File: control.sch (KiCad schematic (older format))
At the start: 1 part

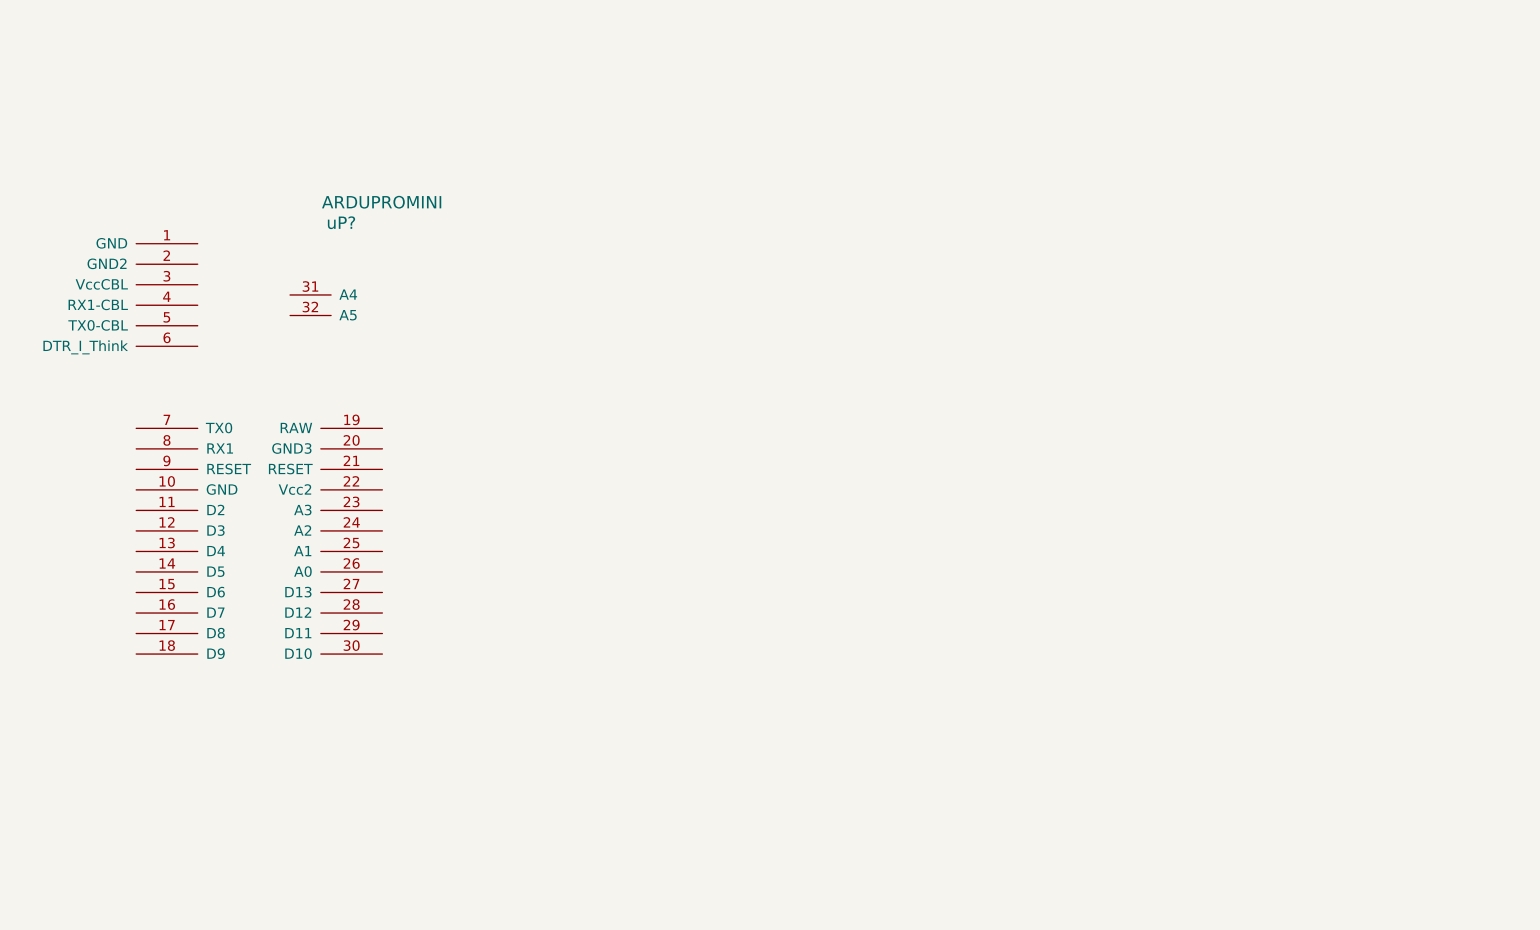
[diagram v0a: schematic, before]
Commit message: Schematic v0.2
Added IC and wiring
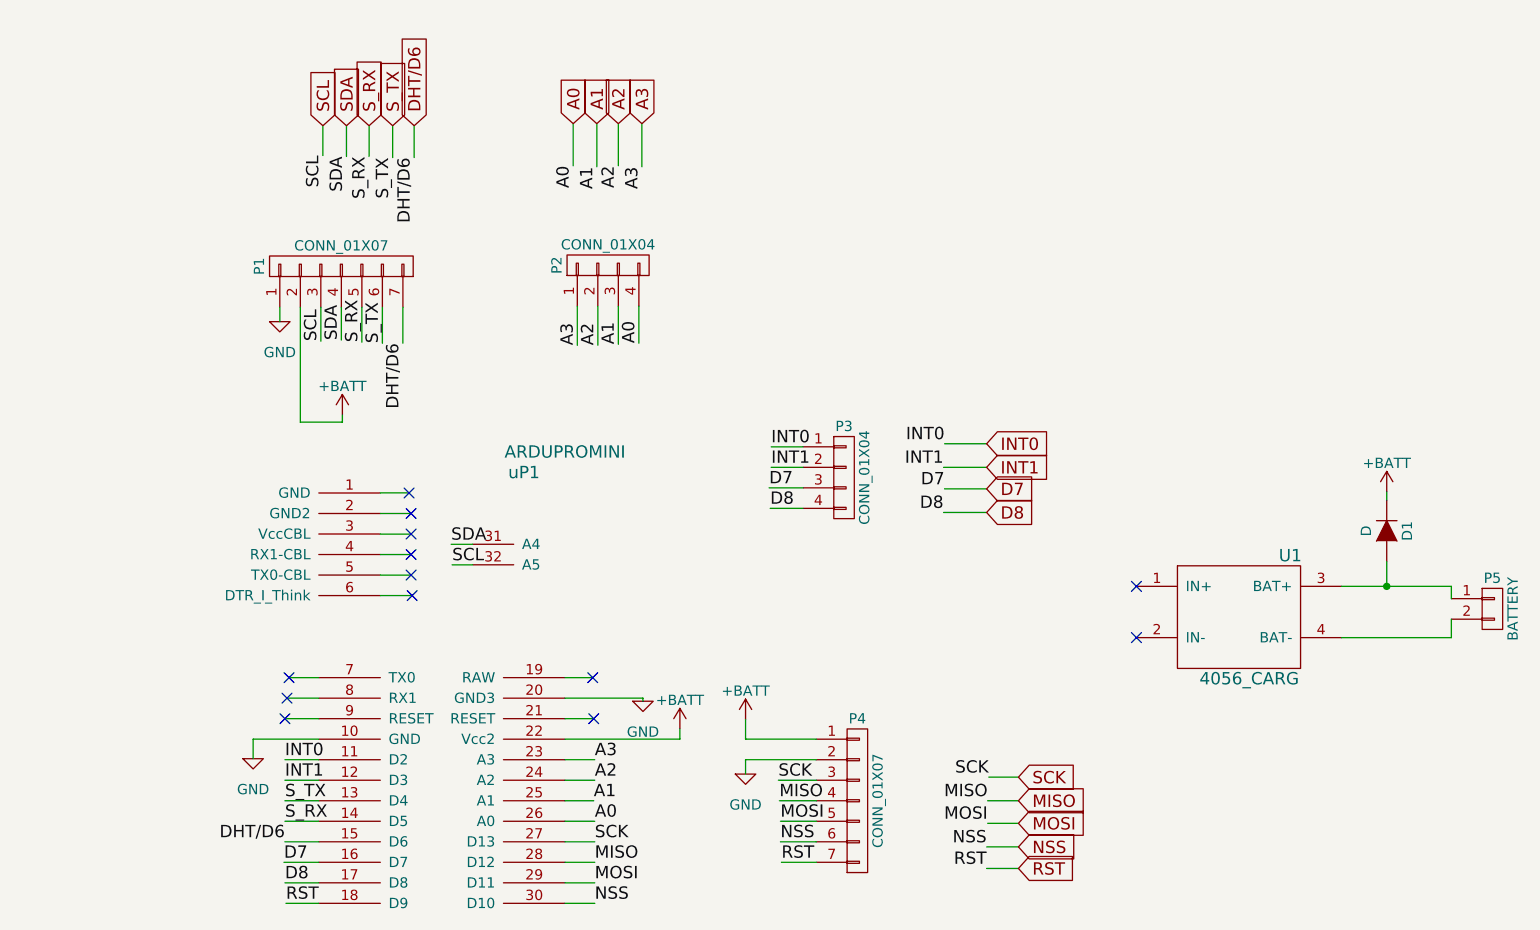
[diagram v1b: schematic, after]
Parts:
- added D1: D, symbol D
- added P1, P4: CONN_01X07, symbol CONN_01X07
- added P2, P3: CONN_01X04, symbol CONN_01X04
- added P5: BATTERY, symbol CONN_01X02
- added U1: 4056_CARG, symbol 4056_CARG
- gave numbers to parts that had none: 1
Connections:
- net GND: now reaches uP1.10 (GND)
- net GND: now also uP1.20 (GND3), P1.1 (P1), P4.2 (P2)
- net INT0: now reaches uP1.11 (D2)
- net INT0: now also P3.1 (P1)
- net INT1: now reaches uP1.12 (D3)
- net INT1: now also P3.2 (P2)
- net S_TX: now reaches uP1.13 (D4)
- net S_TX: now also P1.6 (P6)
- net S_RX: now reaches uP1.14 (D5)
- net S_RX: now also P1.5 (P5)
- net DHT/D6: now reaches uP1.15 (D6)
- net DHT/D6: now also P1.7 (P7)
- net D7: now reaches uP1.16 (D7)
- net D7: now also P3.3 (P3)
- net D8: now reaches uP1.17 (D8)
- net D8: now also P3.4 (P4)
- net RST: now reaches uP1.18 (D9)
- net RST: now also P4.7 (P7)
- net +BATT: now reaches uP1.22 (Vcc2)
- net +BATT: now also D1.1 (K), P1.2 (P2), P4.1 (P1)
- net A3: now reaches uP1.23 (A3)
- net A3: now also P2.1 (P1)
- net A2: now reaches uP1.24 (A2)
- net A2: now also P2.2 (P2)
- net A1: now reaches uP1.25 (A1)
- net A1: now also P2.3 (P3)
- net A0: now reaches uP1.26 (A0)
- net A0: now also P2.4 (P4)
- net SCK: now reaches uP1.27 (D13)
- net SCK: now also P4.3 (P3)
- net MISO: now reaches uP1.28 (D12)
- net MISO: now also P4.4 (P4)
- net MOSI: now reaches uP1.29 (D11)
- net MOSI: now also P4.5 (P5)
- net NSS: now reaches uP1.30 (D10)
- net NSS: now also P4.6 (P6)
- net SDA: now reaches uP1.31 (A4)
- net SDA: now also P1.4 (P4)
- net SCL: now reaches uP1.32 (A5)
- net SCL: now also P1.3 (P3)
- new net: D1.2 (A), P5.1 (P1), U1.3 (BAT+)
- new net: P5.2 (P2), U1.4 (BAT-)
- no-connect marks 0 -> 13
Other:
- moved on the sheet: uP1

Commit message: Fix arduino mini pro pin 6 bug, added capacitors
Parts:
- added C1: C, symbol C
- D1: footprint (none) -> Diodes_ThroughHole:Diode_DO-41_SOD81_Horizontal_RM10
- P1, P4: footprint (none) -> Pin_Headers:Pin_Header_Straight_1x07
- P2, P3: footprint (none) -> Pin_Headers:Pin_Header_Straight_1x04
- P5: footprint (none) -> Pin_Headers:Pin_Header_Straight_1x02
- RAW1: renamed from uP1; footprint (none) -> CatSat:arduinoMiniPro
- U1: footprint (none) -> CatSat:4056_lipoCharg
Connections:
- net +BATT: now also C1.1
- net GND: now also C1.2
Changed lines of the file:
@@
 EESchema Schematic File Version 2
+LIBS:CatSat-rescue
 LIBS:power
 LIBS:device
@@
 LIBS:contrib
 LIBS:valves
-LIBS:ArduProMiniTKB
-LIBS:L80-M39
-LIBS:RFM95W-868S2
-LIBS:theinventorhouse
 LIBS:CatSat-cache
+LIBS:rfm95
 EELAYER 25 0
 EELAYER END
@@
 F 0 "P2" H 4435 2285 50  0000 C CNN
 F 1 "CONN_01X04" V 4535 2035 50  0000 C CNN
-F 2 "" H 4435 2035 50  0000 C CNN
+F 2 "Pin_Headers:Pin_Header_Straight_1x04" H 4435 2035 50  0001 C CNN
 F 3 "" H 4435 2035 50  0000 C CNN
 	1    4435 2035
@@
 F 0 "P1" H 3135 2440 50  0000 C CNN
 F 1 "CONN_01X07" V 3235 2040 50  0000 C CNN
-F 2 "" H 3135 2040 50  0000 C CNN
+F 2 "Pin_Headers:Pin_Header_Straight_1x07" H 3135 2040 50  0001 C CNN
 F 3 "" H 3135 2040 50  0000 C CNN
 	1    3135 2040
@@
 F 0 "P4" H 5650 5045 50  0000 C CNN
 F 1 "CONN_01X07" V 5750 4645 50  0000 C CNN
-F 2 "" H 5650 4645 50  0000 C CNN
+F 2 "Pin_Headers:Pin_Header_Straight_1x07" H 5650 4645 50  0001 C CNN
 F 3 "" H 5650 4645 50  0000 C CNN
 	1    5650 4645
@@
 F 0 "P3" H 5585 3320 50  0000 C CNN
 F 1 "CONN_01X04" V 5685 3070 50  0000 C CNN
-F 2 "" H 5585 3070 50  0000 C CNN
+F 2 "Pin_Headers:Pin_Header_Straight_1x04" H 5585 3070 50  0001 C CNN
 F 3 "" H 5585 3070 50  0000 C CNN
 	1    5585 3070
@@
 NoConn ~ 3480 3645
 $Comp
-L ARDUPROMINI uP1
+L ARDUPROMINI RAW1
 U 1 1 579665C1
 P 4225 2945
-F 0 "uP1" H 4025 2845 60  0000 C CNN
+F 0 "RAW1" H 4025 2845 60  0000 C CNN
 F 1 "ARDUPROMINI" H 4225 2945 60  0000 C CNN
-F 2 "" H 4225 2945 60  0000 C CNN
+F 2 "CatSat:arduinoMiniPro" H 4225 2945 60  0001 C CNN
 F 3 "" H 4225 2945 60  0000 C CNN
 	1    4225 2945
@@
 U 1 1 579865C8
 P 4605 4160
+AR Path="/579865C8" Ref="#PWR03"  Part="1"
+AR Path="/57965E31/579865C8" Ref="#PWR03"  Part="1"
 F 0 "#PWR03" H 4605 3910 50  0001 C CNN
 F 1 "GND" H 4605 4010 50  0000 C CNN
@@
 U 1 1 579869BC
 P 2705 4440
+AR Path="/579869BC" Ref="#PWR04"  Part="1"
+AR Path="/57965E31/579869BC" Ref="#PWR04"  Part="1"
 F 0 "#PWR04" H 2705 4190 50  0001 C CNN
 F 1 "GND" H 2705 4290 50  0000 C CNN
@@
 F 0 "U1" H 7760 4050 60  0000 C CNN
 F 1 "4056_CARG" H 7560 3450 60  0000 C CNN
-F 2 "" H 7510 3750 60  0000 C CNN
+F 2 "CatSat:4056_lipoCharg" H 7510 3750 60  0001 C CNN
 F 3 "" H 7510 3750 60  0000 C CNN
 	1    7510 3750
@@
 F 0 "P5" H 8745 3860 50  0000 C CNN
 F 1 "BATTERY" V 8845 3710 50  0000 C CNN
-F 2 "" H 8745 3710 50  0000 C CNN
+F 2 "Pin_Headers:Pin_Header_Straight_1x02" H 8745 3710 50  0001 C CNN
 F 3 "" H 8745 3710 50  0000 C CNN
 	1    8745 3710
@@
 F 0 "D1" H 8230 3430 50  0000 C CNN
 F 1 "D" H 8230 3230 50  0000 C CNN
-F 2 "" H 8230 3330 50  0000 C CNN
+F 2 "Diodes_ThroughHole:Diode_DO-41_SOD81_Horizontal_RM10" H 8230 3330 50  0001 C CNN
 F 3 "" H 8230 3330 50  0000 C CNN
 	1    8230 3330
@@
 U 1 1 5798B584
 P 2835 2310
+AR Path="/5798B584" Ref="#PWR06"  Part="1"
+AR Path="/57965E31/5798B584" Ref="#PWR06"  Part="1"
 F 0 "#PWR06" H 2835 2060 50  0001 C CNN
 F 1 "GND" H 2835 2160 50  0000 C CNN
@@
 U 1 1 579A7004
 P 5105 4515
+AR Path="/579A7004" Ref="#PWR07"  Part="1"
+AR Path="/57965E31/579A7004" Ref="#PWR07"  Part="1"
 F 0 "#PWR07" H 5105 4265 50  0001 C CNN
 F 1 "GND" H 5105 4365 50  0000 C CNN
@@
 Wire Wire Line
 	5105 4345 5105 4250
+$Comp
+L C C1
+U 1 1 579BC305
+P 6955 2585
+F 0 "C1" H 6980 2685 50  0000 L CNN
+F 1 "C" H 6980 2485 50  0000 L CNN
+F 2 "" H 6993 2435 30  0000 C CNN
+F 3 "" H 6955 2585 60  0000 C CNN
+	1    6955 2585
+	1    0    0    -1
+$EndComp
+$Comp
+L +BATT #PWR?
+U 1 1 579BC449
+P 6955 2385
+F 0 "#PWR?" H 6955 2235 50  0001 C CNN
+F 1 "+BATT" H 6955 2525 50  0000 C CNN
+F 2 "" H 6955 2385 50  0000 C CNN
+F 3 "" H 6955 2385 50  0000 C CNN
+	1    6955 2385
+	1    0    0    -1
+$EndComp
+$Comp
+L GND #PWR?
+U 1 1 579BC6D3
+P 6955 2785
+AR Path="/579BC6D3" Ref="#PWR?"  Part="1"
+AR Path="/57965E31/579BC6D3" Ref="#PWR?"  Part="1"
+F 0 "#PWR?" H 6955 2535 50  0001 C CNN
+F 1 "GND" H 6955 2635 50  0000 C CNN
+F 2 "" H 6955 2785 50  0000 C CNN
+F 3 "" H 6955 2785 50  0000 C CNN
+	1    6955 2785
+	1    0    0    -1
+$EndComp
+Wire Wire Line
+	6955 2735 6955 2785
+Wire Wire Line
+	6955 2385 6955 2435
 $EndSCHEMATC

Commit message: Finished telemtry PCB
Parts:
- C1: footprint (none) -> Capacitors_ThroughHole:C_Disc_D6_P5
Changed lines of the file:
@@
 F 0 "C1" H 6980 2685 50  0000 L CNN
 F 1 "C" H 6980 2485 50  0000 L CNN
-F 2 "" H 6993 2435 30  0000 C CNN
+F 2 "Capacitors_ThroughHole:C_Disc_D6_P5" H 6993 2435 30  0001 C CNN
 F 3 "" H 6955 2585 60  0000 C CNN
 	1    6955 2585
@@
 $EndComp
 $Comp
-L +BATT #PWR?
+L +BATT #PWR09
 U 1 1 579BC449
 P 6955 2385
-F 0 "#PWR?" H 6955 2235 50  0001 C CNN
+F 0 "#PWR09" H 6955 2235 50  0001 C CNN
 F 1 "+BATT" H 6955 2525 50  0000 C CNN
 F 2 "" H 6955 2385 50  0000 C CNN
@@
 P 6955 2785
 AR Path="/579BC6D3" Ref="#PWR?"  Part="1"
-AR Path="/57965E31/579BC6D3" Ref="#PWR?"  Part="1"
-F 0 "#PWR?" H 6955 2535 50  0001 C CNN
+AR Path="/57965E31/579BC6D3" Ref="#PWR010"  Part="1"
+F 0 "#PWR010" H 6955 2535 50  0001 C CNN
 F 1 "GND" H 6955 2635 50  0000 C CNN
 F 2 "" H 6955 2785 50  0000 C CNN

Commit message: PCB final
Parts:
- added P0n1: ON, Pin_Headers:Pin_Header_Straight_1x02, symbol CONN_01X02
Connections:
- net +BATT: now also P0n1.1 (P1); no longer D1.1 (K)
- new net: D1.1 (K), P0n1.2 (P2)
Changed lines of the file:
@@
 L D D1
 U 1 1 579882B5
-P 8230 3330
-F 0 "D1" H 8230 3430 50  0000 C CNN
-F 1 "D" H 8230 3230 50  0000 C CNN
-F 2 "Diodes_ThroughHole:Diode_DO-41_SOD81_Horizontal_RM10" H 8230 3330 50  0001 C CNN
-F 3 "" H 8230 3330 50  0000 C CNN
-	1    8230 3330
+P 8225 3340
+F 0 "D1" H 8225 3440 50  0000 C CNN
+F 1 "D" H 8225 3240 50  0000 C CNN
+F 2 "Diodes_ThroughHole:Diode_DO-41_SOD81_Horizontal_RM10" H 8225 3340 50  0001 C CNN
+F 3 "" H 8225 3340 50  0000 C CNN
+	1    8225 3340
 	0    1    1    0
 $EndComp
@@
 L +BATT #PWR05
 U 1 1 5798845B
-P 8230 3140
-F 0 "#PWR05" H 8230 2990 50  0001 C CNN
-F 1 "+BATT" H 8230 3280 50  0000 C CNN
-F 2 "" H 8230 3140 50  0000 C CNN
-F 3 "" H 8230 3140 50  0000 C CNN
-	1    8230 3140
+P 8260 2875
+F 0 "#PWR05" H 8260 2725 50  0001 C CNN
+F 1 "+BATT" H 8260 3015 50  0000 C CNN
+F 2 "" H 8260 2875 50  0000 C CNN
+F 3 "" H 8260 2875 50  0000 C CNN
+	1    8260 2875
 	1    0    0    -1
 $EndComp
@@
 	4785 4345 4785 4295
 Wire Wire Line
-	8010 3600 8545 3600
-Wire Wire Line
 	8545 3600 8545 3660
 Wire Wire Line
@@
 Wire Wire Line
 	8545 3850 8010 3850
-Connection ~ 8230 3600
-Wire Wire Line
-	8230 3480 8230 3600
-Wire Wire Line
-	8230 3600 8235 3600
-Wire Wire Line
-	8230 3140 8230 3180
+Wire Wire Line
+	8235 3600 8230 3600
+Wire Wire Line
+	8260 2875 8260 2995
 Wire Wire Line
 	2935 2240 2935 2800
@@
 Wire Wire Line
 	6955 2385 6955 2435
+Wire Wire Line
+	8235 3490 8235 3600
+Connection ~ 8235 3600
+Wire Wire Line
+	8010 3600 8545 3600
+$Comp
+L CONN_01X02 P0n1
+U 1 1 57A00135
+P 8470 3045
+F 0 "P0n1" H 8470 3195 50  0000 C CNN
+F 1 "ON" V 8570 3045 50  0000 C CNN
+F 2 "Pin_Headers:Pin_Header_Straight_1x02" H 8470 3045 50  0001 C CNN
+F 3 "" H 8470 3045 50  0000 C CNN
+	1    8470 3045
+	1    0    0    -1
+$EndComp
+Wire Wire Line
+	8260 2995 8270 2995
+Wire Wire Line
+	8270 3095 8225 3095
+Wire Wire Line
+	8225 3095 8225 3190
+Wire Wire Line
+	8235 3490 8225 3490
 $EndSCHEMATC

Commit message: Fix Source Track
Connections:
- net GND: now also P5.2 (P2), U1.4 (BAT-)
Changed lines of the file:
@@
 LIBS:valves
 LIBS:CatSat-cache
-LIBS:rfm95
 EELAYER 25 0
 EELAYER END
@@
 encoding utf-8
 Sheet 2 4
-Title ""
-Date "2016-07-26"
+Title "CatSat v1.0"
+Date "2016-08-10"
 Rev "0.2"
 Comp "Electronic Cats"
@@
 Wire Wire Line
 	8235 3490 8225 3490
+$Comp
+L GND #PWR?
+U 1 1 57AC0CD8
+P 8180 4085
+F 0 "#PWR?" H 8180 3835 50  0001 C CNN
+F 1 "GND" H 8180 3935 50  0000 C CNN
+F 2 "" H 8180 4085 50  0000 C CNN
+F 3 "" H 8180 4085 50  0000 C CNN
+	1    8180 4085
+	1    0    0    -1
+$EndComp
+Wire Wire Line
+	8180 4085 8180 3850
+Connection ~ 8180 3850
 $EndSCHEMATC
